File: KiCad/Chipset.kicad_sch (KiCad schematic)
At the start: 8 parts, among them U2 OPTi_82C895, U3 OPTi_82C602, U401 74F32, Y1 32768Hz

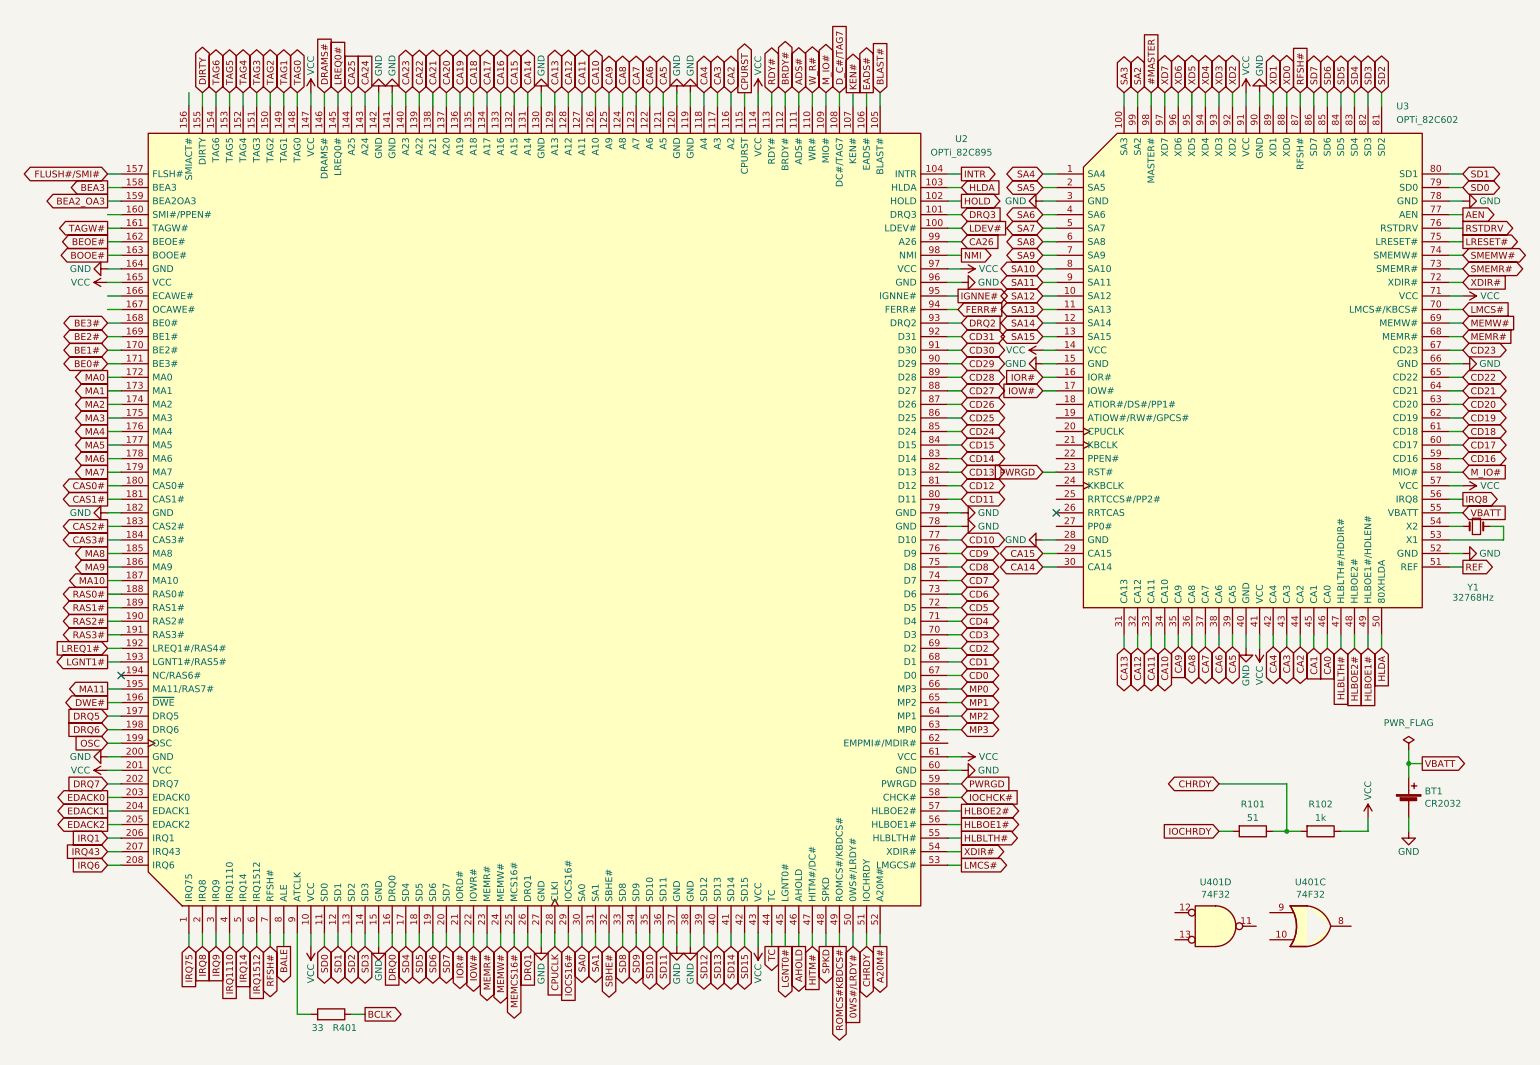
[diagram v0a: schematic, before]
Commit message: Version 0.2: Update cache schematic
Signed-off-by: Sergey Kiselev <sergey.kiselev@intel.com>
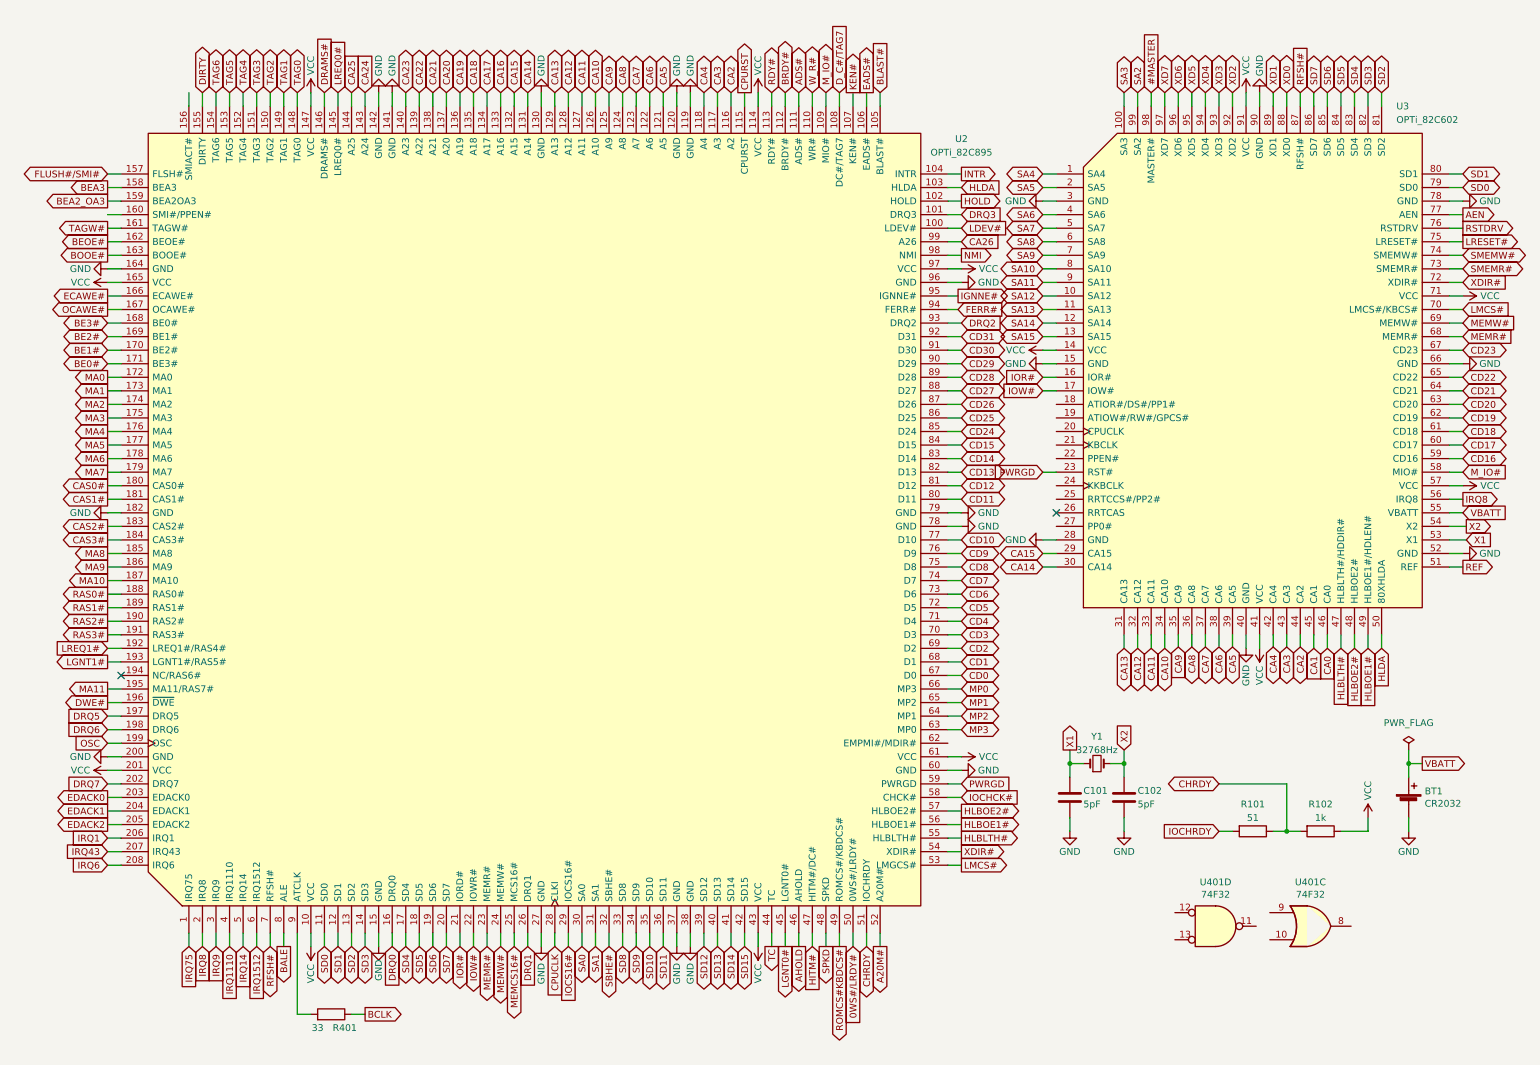
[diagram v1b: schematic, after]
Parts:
- added C101, C102: 5pF, symbol Device:C
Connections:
- net GND: now also C101.2, C102.2
- net X1: now reaches Y1.1
- net X1: now also U3.53 (X1), C101.1; no longer U3.54 (X2)
- net X2: now reaches Y1.2
- net X2: now also U3.54 (X2), C102.1; no longer U3.53 (X1)
- net ECAWE#: now reaches U2.166 (ECAWE#)
- net OCAWE#: now reaches U2.167 (OCAWE#)
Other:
- moved on the sheet: Y1
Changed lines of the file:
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@@
     (title "486 Sandy River Motherboard")
   )
+  (junction (at 203.2 146.05) (diameter 0) (color 0 0 0 0)
+  )
+  (junction (at 213.36 146.05) (diameter 0) (color 0 0 0 0)
+  )
   (junction (at 266.7 146.05) (diameter 0) (color 0 0 0 0)
   )
@@
     (stroke (width 0) (type default) (color 0 0 0 0))
   )
-  (wire (pts (xy 284.48 101.6) (xy 281.94 101.6))
+  (wire (pts (xy 213.36 146.05) (xy 210.82 146.05))
     (stroke (width 0) (type default) (color 0 0 0 0))
   )
@@
     (stroke (width 0) (type default) (color 0 0 0 0))
   )
-  (wire (pts (xy 274.32 101.6) (xy 276.86 101.6))
+  (wire (pts (xy 203.2 146.05) (xy 205.74 146.05))
     (stroke (width 0) (type default) (color 0 0 0 0))
   )
@@
     (stroke (width 0) (type default) (color 0 0 0 0))
   )
-  (wire (pts (xy 284.48 104.14) (xy 284.48 101.6))
+  (wire (pts (xy 213.36 148.59) (xy 213.36 146.05))
     (stroke (width 0) (type default) (color 0 0 0 0))
   )
@@
     (stroke (width 0) (type default) (color 0 0 0 0))
   )
+  (wire (pts (xy 213.36 158.75) (xy 213.36 156.21))
+    (stroke (width 0) (type default) (color 0 0 0 0))
+  )
   (wire (pts (xy 200.66 45.72) (xy 198.12 45.72))
     (stroke (width 0) (type default) (color 0 0 0 0))
@@
     (stroke (width 0) (type default) (color 0 0 0 0))
   )
+  (wire (pts (xy 203.2 146.05) (xy 203.2 148.59))
+    (stroke (width 0) (type default) (color 0 0 0 0))
+  )
   (wire (pts (xy 60.96 20.32) (xy 60.96 22.86))
     (stroke (width 0) (type default) (color 0 0 0 0))
@@
     (stroke (width 0) (type default) (color 0 0 0 0))
   )
+  (wire (pts (xy 203.2 143.51) (xy 203.2 146.05))
+    (stroke (width 0) (type default) (color 0 0 0 0))
+  )
   (wire (pts (xy 22.86 139.7) (xy 25.4 139.7))
     (stroke (width 0) (type default) (color 0 0 0 0))
@@
     (stroke (width 0) (type default) (color 0 0 0 0))
   )
+  (wire (pts (xy 274.32 104.14) (xy 277.495 104.14))
+    (stroke (width 0) (type default) (color 0 0 0 0))
+  )
   (wire (pts (xy 198.12 106.68) (xy 200.66 106.68))
     (stroke (width 0) (type default) (color 0 0 0 0))
@@
     (stroke (width 0) (type default) (color 0 0 0 0))
   )
+  (wire (pts (xy 274.32 101.6) (xy 277.495 101.6))
+    (stroke (width 0) (type default) (color 0 0 0 0))
+  )
   (wire (pts (xy 180.34 93.98) (xy 182.88 93.98))
     (stroke (width 0) (type default) (color 0 0 0 0))
@@
     (stroke (width 0) (type default) (color 0 0 0 0))
   )
-  (wire (pts (xy 274.32 104.14) (xy 284.48 104.14))
-    (stroke (width 0) (type default) (color 0 0 0 0))
-  )
   (wire (pts (xy 73.66 20.32) (xy 73.66 22.86))
     (stroke (width 0) (type default) (color 0 0 0 0))
@@
     (stroke (width 0) (type default) (color 0 0 0 0))
   )
+  (wire (pts (xy 203.2 158.75) (xy 203.2 156.21))
+    (stroke (width 0) (type default) (color 0 0 0 0))
+  )
   (wire (pts (xy 22.86 53.34) (xy 25.4 53.34))
     (stroke (width 0) (type default) (color 0 0 0 0))
@@
     (stroke (width 0) (type default) (color 0 0 0 0))
   )
+  (wire (pts (xy 213.36 143.51) (xy 213.36 146.05))
+    (stroke (width 0) (type default) (color 0 0 0 0))
+  )
   (wire (pts (xy 119.38 180.34) (xy 119.38 177.8))
     (stroke (width 0) (type default) (color 0 0 0 0))
@@
     )
   )
+  (global_label "X1" (shape output) (at 203.2 143.51 90) (fields_autoplaced)
+    (effects (font (size 1.27 1.27)) (justify left))
+    (property "Intersheet References" "${INTERSHEET_REFS}" (id 0) (at 203.1206 138.7668 90)
+      (effects (font (size 1.27 1.27)) (justify left) hide)
+    )
+  )
   (global_label "DRQ3" (shape input) (at 182.88 43.18 0) (fields_autoplaced)
     (effects (font (size 1.27 1.27)) (justify left))
@@
     )
   )
+  (global_label "X2" (shape input) (at 213.36 143.51 90) (fields_autoplaced)
+    (effects (font (size 1.27 1.27)) (justify left))
+    (property "Intersheet References" "${INTERSHEET_REFS}" (id 0) (at 213.2806 138.7668 90)
+      (effects (font (size 1.27 1.27)) (justify left) hide)
+    )
+  )
   (global_label "CA25" (shape input) (at 68.58 20.32 90) (fields_autoplaced)
     (effects (font (size 1.27 1.27)) (justify left))
@@
     )
   )
+  (global_label "OCAWE#" (shape output) (at 22.86 60.96 180) (fields_autoplaced)
+    (effects (font (size 1.27 1.27)) (justify right))
+    (property "Intersheet References" "${INTERSHEET_REFS}" (id 0) (at 12.9763 60.8806 0)
+      (effects (font (size 1.27 1.27)) (justify right) hide)
+    )
+  )
   (global_label "DRQ1" (shape input) (at 101.6 180.34 270) (fields_autoplaced)
     (effects (font (size 1.27 1.27)) (justify right))
@@
     )
   )
+  (global_label "X2" (shape output) (at 277.495 101.6 0) (fields_autoplaced)
+    (effects (font (size 1.27 1.27)) (justify left))
+    (property "Intersheet References" "${INTERSHEET_REFS}" (id 0) (at 282.2382 101.5206 0)
+      (effects (font (size 1.27 1.27)) (justify left) hide)
+    )
+  )
   (global_label "REF" (shape output) (at 276.86 109.22 0) (fields_autoplaced)
     (effects (font (size 1.27 1.27)) (justify left))
@@
     )
   )
+  (global_label "X1" (shape input) (at 277.495 104.14 0) (fields_autoplaced)
+    (effects (font (size 1.27 1.27)) (justify left))
+    (property "Intersheet References" "${INTERSHEET_REFS}" (id 0) (at 282.2382 104.0606 0)
+      (effects (font (size 1.27 1.27)) (justify left) hide)
+    )
+  )
   (global_label "HLDA" (shape input) (at 182.88 38.1 0) (fields_autoplaced)
     (effects (font (size 1.27 1.27)) (justify left))
@@
     )
   )
+  (global_label "ECAWE#" (shape output) (at 22.86 58.42 180) (fields_autoplaced)
+    (effects (font (size 1.27 1.27)) (justify right))
+    (property "Intersheet References" "${INTERSHEET_REFS}" (id 0) (at 13.1577 58.3406 0)
+      (effects (font (size 1.27 1.27)) (justify right) hide)
+    )
+  )
   (symbol (lib_id "power:GND") (at 129.54 180.34 0) (unit 1)
     (in_bom yes) (on_board yes)
@@
     (pin "1")
   )
+  (symbol (lib_id "power:GND") (at 203.2 158.75 0) (unit 1)
+    (in_bom yes) (on_board yes)
+    (property "Reference" "#PWR0155" (id 0) (at 203.2 165.1 0)
+      (effects (font (size 1.27 1.27)) hide)
+    )
+    (property "Value" "GND" (id 1) (at 203.2 162.56 0))
+    (property "Footprint" "" (id 2) (at 203.2 158.75 0)
+      (effects (font (size 1.27 1.27)) hide)
+    )
+    (property "Datasheet" "" (id 3) (at 203.2 158.75 0)
+      (effects (font (size 1.27 1.27)) hide)
+    )
+    (pin "1")
+  )
   (symbol (lib_id "power:GND") (at 76.2 20.32 180) (unit 1)
     (in_bom yes) (on_board yes)
@@
     (pin "1")
   )
-  (symbol (lib_id "Device:Crystal_Small") (at 279.4 101.6 0) (unit 1)
+  (symbol (lib_id "Device:Crystal_Small") (at 208.28 146.05 0) (unit 1)
     (in_bom yes) (on_board yes)
-    (property "Reference" "Y1" (id 0) (at 278.765 113.03 0))
-    (property "Value" "32768Hz" (id 1) (at 278.765 114.935 0))
-    (property "Footprint" "" (id 2) (at 279.4 101.6 0)
+    (property "Reference" "Y1" (id 0) (at 208.28 140.97 0))
+    (property "Value" "32768Hz" (id 1) (at 208.28 143.51 0))
+    (property "Footprint" "" (id 2) (at 208.28 146.05 0)
       (effects (font (size 1.27 1.27)) hide)
     )
-    (property "Datasheet" "~" (id 3) (at 279.4 101.6 0)
+    (property "Datasheet" "~" (id 3) (at 208.28 146.05 0)
       (effects (font (size 1.27 1.27)) hide)
     )
@@
     (pin "1")
   )
+  (symbol (lib_id "power:GND") (at 213.36 158.75 0) (unit 1)
+    (in_bom yes) (on_board yes)
+    (property "Reference" "#PWR0156" (id 0) (at 213.36 165.1 0)
+      (effects (font (size 1.27 1.27)) hide)
+    )
+    (property "Value" "GND" (id 1) (at 213.36 162.56 0))
+    (property "Footprint" "" (id 2) (at 213.36 158.75 0)
+      (effects (font (size 1.27 1.27)) hide)
+    )
+    (property "Datasheet" "" (id 3) (at 213.36 158.75 0)
+      (effects (font (size 1.27 1.27)) hide)
+    )
+    (pin "1")
+  )
   (symbol (lib_id "power:VCC") (at 198.12 68.58 90) (unit 1)
     (in_bom yes) (on_board yes)
@@
     (pin "1")
   )
+  (symbol (lib_id "Device:C") (at 213.36 152.4 0) (unit 1)
+    (in_bom yes) (on_board yes)
+    (property "Reference" "C102" (id 0) (at 215.9 151.13 0)
+      (effects (font (size 1.27 1.27)) (justify left))
+    )
+    (property "Value" "5pF" (id 1) (at 215.9 153.67 0)
+      (effects (font (size 1.27 1.27)) (justify left))
+    )
+    (property "Footprint" "" (id 2) (at 214.3252 156.21 0)
+      (effects (font (size 1.27 1.27)) hide)
+    )
+    (property "Datasheet" "~" (id 3) (at 213.36 152.4 0)
+      (effects (font (size 1.27 1.27)) hide)
+    )
+    (pin "1")
+    (pin "2")
+  )
   (symbol (lib_id "power:GND") (at 276.86 106.68 90) (unit 1)
     (in_bom yes) (on_board yes)
@@
     (pin "1")
   )
+  (symbol (lib_id "Device:C") (at 203.2 152.4 0) (unit 1)
+    (in_bom yes) (on_board yes)
+    (property "Reference" "C101" (id 0) (at 205.74 151.13 0)
+      (effects (font (size 1.27 1.27)) (justify left))
+    )
+    (property "Value" "5pF" (id 1) (at 205.74 153.67 0)
+      (effects (font (size 1.27 1.27)) (justify left))
+    )
+    (property "Footprint" "" (id 2) (at 204.1652 156.21 0)
+      (effects (font (size 1.27 1.27)) hide)
+    )
+    (property "Datasheet" "~" (id 3) (at 203.2 152.4 0)
+      (effects (font (size 1.27 1.27)) hide)
+    )
+    (pin "1")
+    (pin "2")
+  )
 )

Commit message: Version 0.3: Update DRAM schematic, pull-ups/pull-downs, CPU configuration jumpers
Signed-off-by: Sergey Kiselev <skiselev@gmail.com>
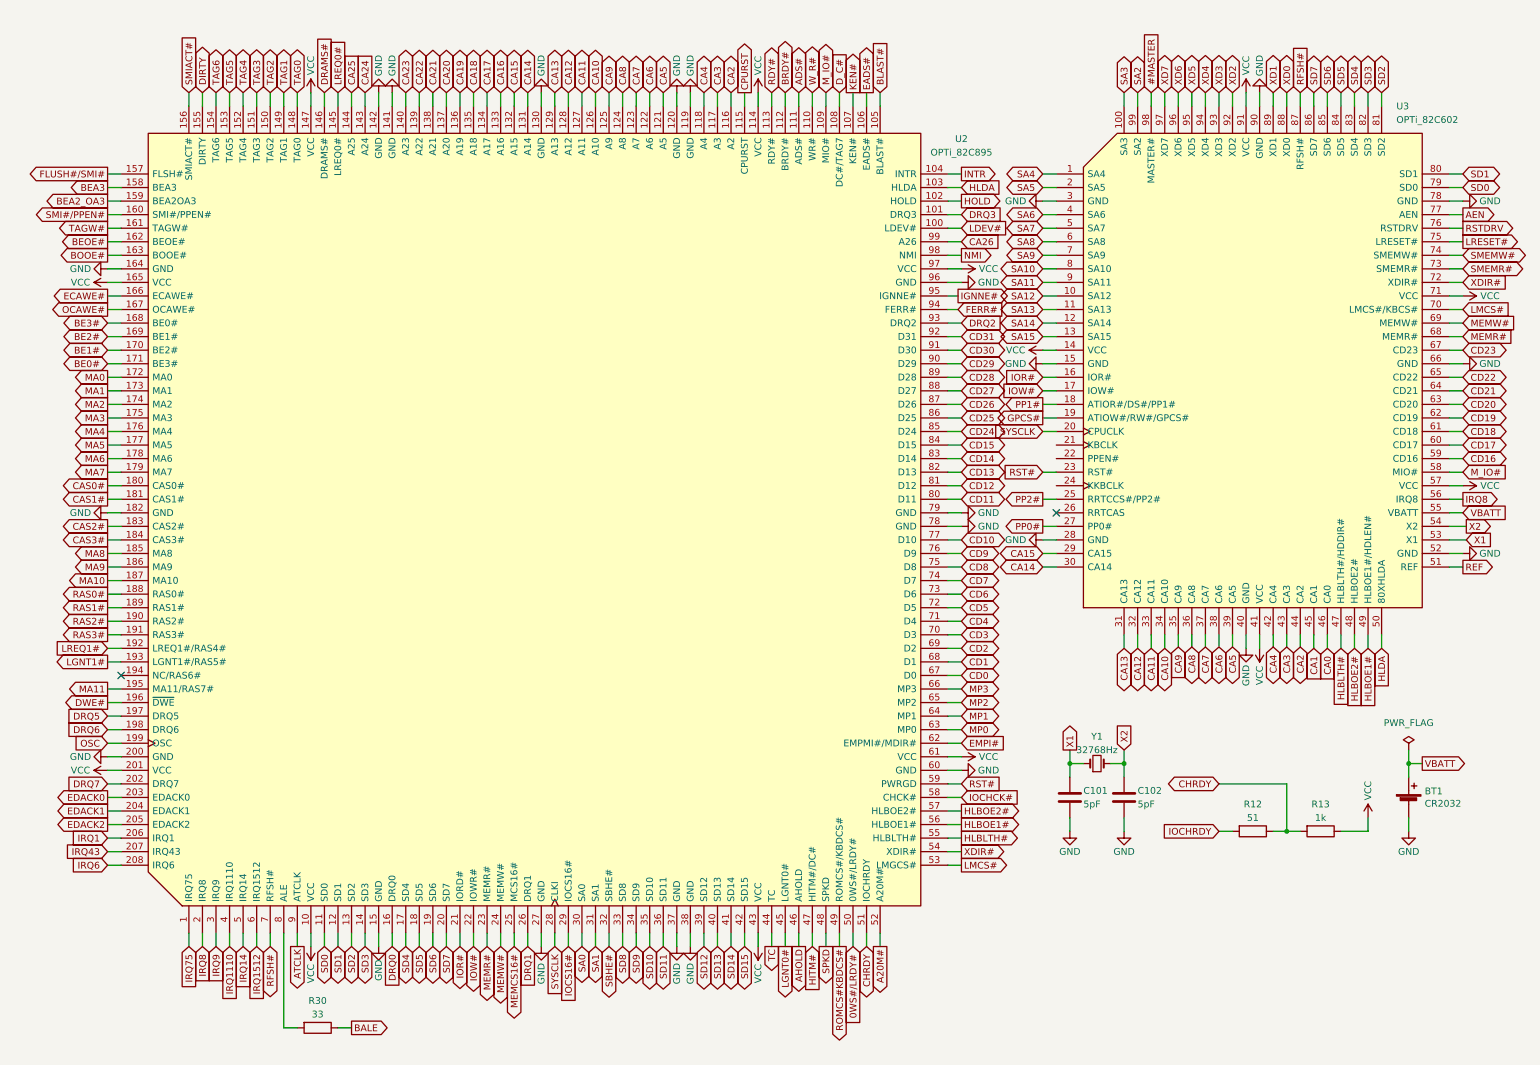
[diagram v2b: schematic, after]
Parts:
- removed R401: 33, symbol Device:R
- removed U401: 74F32, symbol 74xx:74LS32
- added R30: 33, symbol Device:R
- renumbered R101 to R12, R102 to R13
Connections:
- net CPUCLK is gone; now on net SYSCLK: U2.28 (CLKI)
- net BALE: now also R30.1; no longer U2.8 (ALE)
- net MP0: now also U2.63 (MP0); no longer U2.66 (MP3)
- net MP1: now also U2.64 (MP1); no longer U2.65 (MP2)
- net MP2: now also U2.65 (MP2); no longer U2.64 (MP1)
- net MP3: now also U2.66 (MP3); no longer U2.63 (MP0)
- net ATCLK: now reaches U2.9 (ATCLK)
- net PP1#: now reaches U3.18 (ATIOR#/DS#/PP1#)
- net GPCS#: now reaches U3.19 (ATIOW#/RW#/GPCS#)
- net SYSCLK: now reaches U3.20 (CPUCLK)
- net PP2#: now reaches U3.25 (RRTCCS#/PP2#)
- net PP0#: now reaches U3.27 (PP0#)
- net SMIACT#: now reaches U2.156 (SMIACT#)
- net SMI#/PPEN#: now reaches U2.160 (SMI#/PPEN#)
- net EMPI#: now reaches U2.62 (EMPMI#/MDIR#)
- net D_C#/TAG7 renamed D_C#
- net PWRGD renamed RST#
- new net: R30.2, U2.8 (ALE)
